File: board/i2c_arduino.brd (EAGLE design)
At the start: 36.5 x 55.9 mm, 20 parts, among them IC1 MEGA8-P

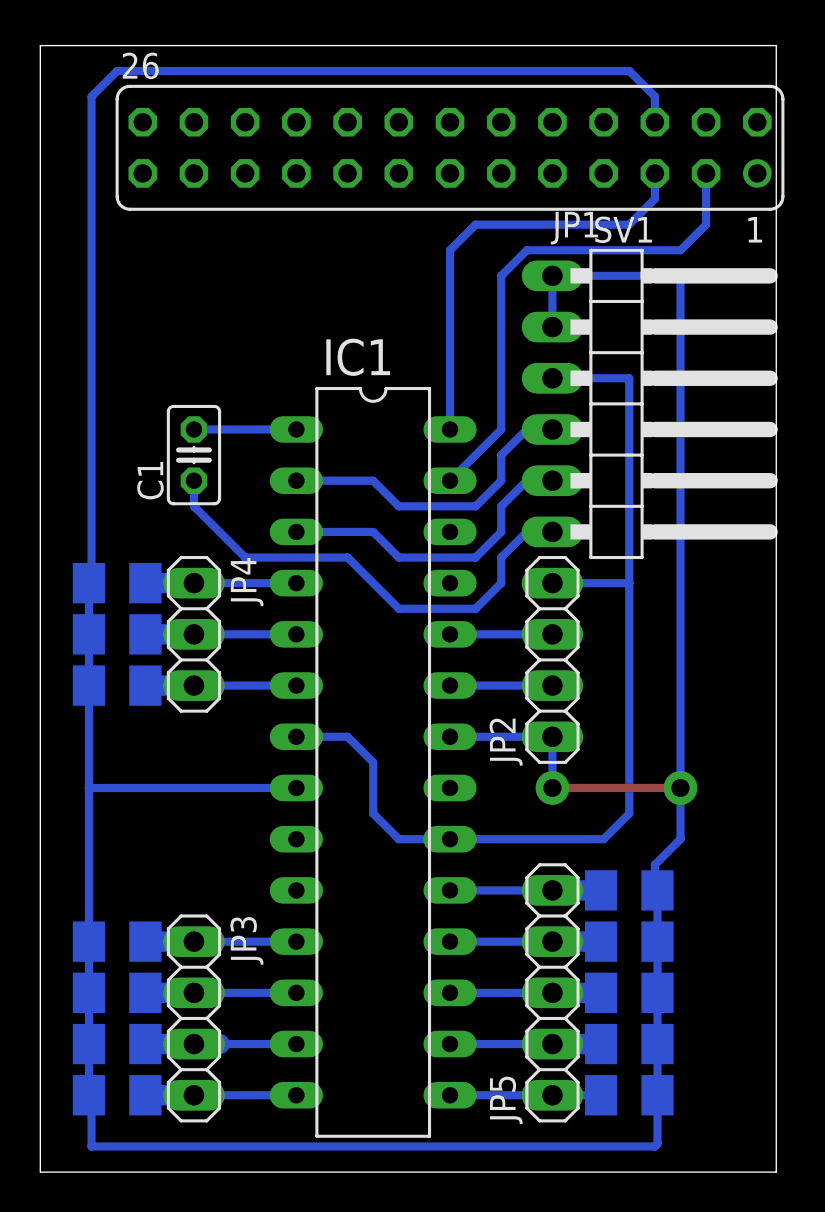
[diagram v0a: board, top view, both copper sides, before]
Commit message: Updated buttons handling
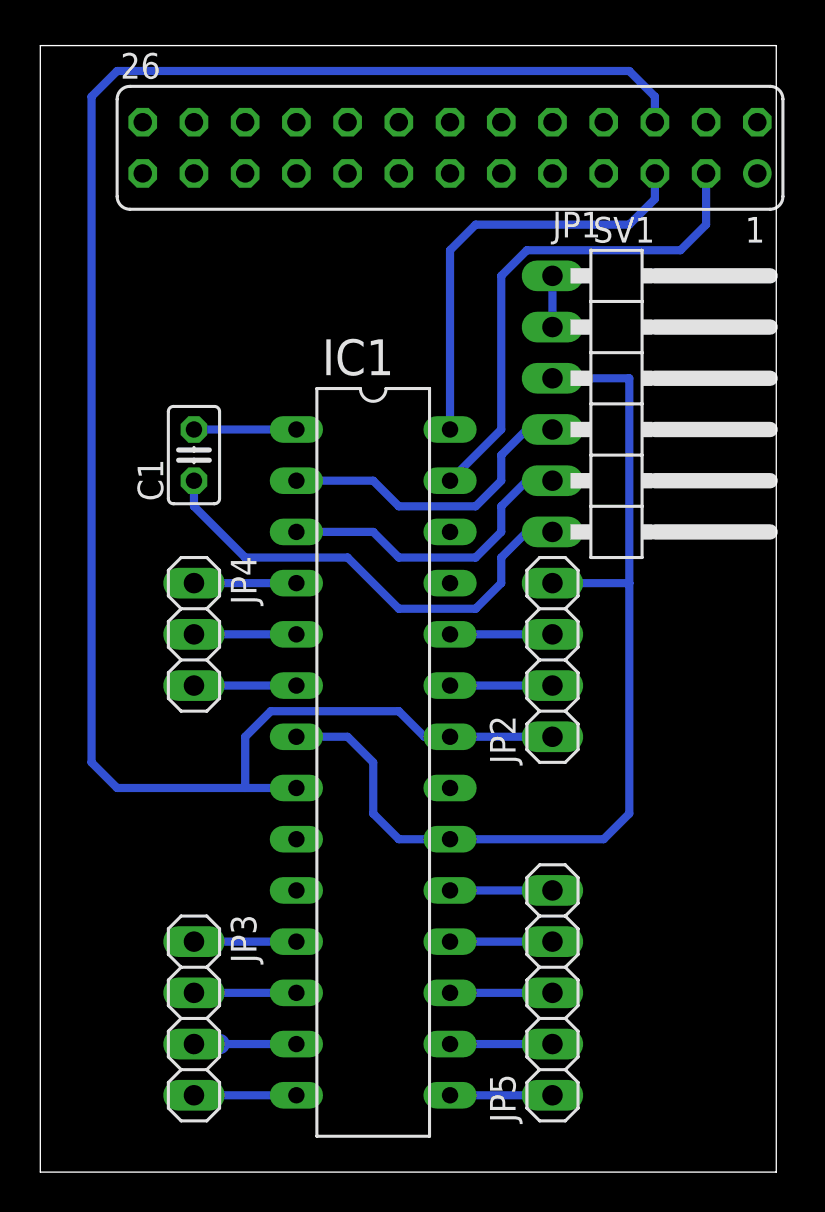
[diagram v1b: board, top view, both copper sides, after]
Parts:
- removed R1, R10, R11, R12, R2, R3, R4, R5, R6, R7, R8, R9: 10k, rcl:M1206
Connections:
- net GND: no longer R1.1, R10.1, R11.1, R12.1, R2.1, R3.1, R4.1, R5.1, R6.1, R7.1, R8.1, R9.1
- net IN10: no longer R9.2
- net IN11: no longer R10.2
- net IN12: no longer R11.2
- net IN13: no longer R12.2
- net IN2: no longer R1.2
- net IN3: no longer R3.2
- net IN4: no longer R2.2
- net IN5: no longer R4.2
- net IN6: no longer R5.2
- net IN7: no longer R6.2
- net IN8: no longer R7.2
- net IN9: no longer R8.2
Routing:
- net GND: track 187.3 -> 95.3 mm, vias 2 -> 0
- net IN9: track 7.49 -> 5.08 mm
- net IN8: track 7.49 -> 5.08 mm
- net IN7: track 8.76 -> 6.35 mm
- net IN6: track 7.49 -> 5.08 mm
- net IN5: track 7.49 -> 5.08 mm
- net IN4: track 7.49 -> 5.08 mm
- net IN3: track 7.49 -> 5.08 mm
- net IN2: track 7.49 -> 5.08 mm
- net IN13: track 7.49 -> 5.08 mm
- net IN12: track 7.49 -> 5.08 mm
- net IN11: track 7.49 -> 5.08 mm
- net IN10: track 7.49 -> 5.08 mm
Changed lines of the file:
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@@
 <attribute name="OC_FARNELL" value="unknown" x="20.32" y="50.8" size="1.778" layer="27" rot="R180" display="off"/>
 </element>
-<element name="R1" library="rcl" package="M1206" value="10k" x="3.81" y="29.21" rot="MR180"/>
-<element name="R2" library="rcl" package="M1206" value="10k" x="3.81" y="24.13" rot="MR180"/>
-<element name="R3" library="rcl" package="M1206" value="10k" x="3.81" y="26.67" rot="MR180"/>
-<element name="R4" library="rcl" package="M1206" value="10k" x="3.81" y="11.43" rot="MR180"/>
-<element name="R5" library="rcl" package="M1206" value="10k" x="3.81" y="8.89" rot="MR180"/>
-<element name="R6" library="rcl" package="M1206" value="10k" x="3.81" y="6.35" rot="MR180"/>
-<element name="R7" library="rcl" package="M1206" value="10k" x="3.81" y="3.81" rot="MR180"/>
-<element name="R8" library="rcl" package="M1206" value="10k" x="29.21" y="3.81" rot="MR0"/>
-<element name="R9" library="rcl" package="M1206" value="10k" x="29.21" y="6.35" rot="MR0"/>
-<element name="R10" library="rcl" package="M1206" value="10k" x="29.21" y="8.89" rot="MR0"/>
-<element name="R11" library="rcl" package="M1206" value="10k" x="29.21" y="11.43" rot="MR0"/>
-<element name="R12" library="rcl" package="M1206" value="10k" x="29.21" y="13.97" rot="MR0"/>
 <element name="JP2" library="pinhead" package="1X04" value="" x="25.4" y="25.4" rot="R90"/>
 <element name="JP3" library="pinhead" package="1X04" value="" x="7.62" y="7.62" rot="R270"/>
@@
 <contactref element="JP1" pad="1"/>
 <contactref element="IC1" pad="8"/>
-<contactref element="R1" pad="1"/>
-<contactref element="R12" pad="1"/>
-<contactref element="R11" pad="1"/>
-<contactref element="R10" pad="1"/>
-<contactref element="R3" pad="1"/>
-<contactref element="R2" pad="1"/>
-<contactref element="R4" pad="1"/>
-<contactref element="R5" pad="1"/>
-<contactref element="R6" pad="1"/>
-<contactref element="R7" pad="1"/>
-<contactref element="R8" pad="1"/>
-<contactref element="R9" pad="1"/>
-<wire x1="2.41" y1="3.81" x2="2.41" y2="6.35" width="0.4064" layer="16"/>
-<wire x1="2.41" y1="6.35" x2="2.41" y2="8.89" width="0.4064" layer="16"/>
-<wire x1="2.41" y1="8.89" x2="2.41" y2="11.43" width="0.4064" layer="16"/>
-<wire x1="2.41" y1="24.13" x2="2.41" y2="19.05" width="0.4064" layer="16"/>
-<wire x1="2.41" y1="19.05" x2="2.41" y2="11.43" width="0.4064" layer="16"/>
-<wire x1="2.41" y1="26.67" x2="2.41" y2="24.13" width="0.4064" layer="16"/>
-<wire x1="2.41" y1="29.21" x2="2.41" y2="26.67" width="0.4064" layer="16"/>
-<wire x1="30.61" y1="3.81" x2="30.61" y2="1.4" width="0.4064" layer="16"/>
-<wire x1="30.61" y1="1.4" x2="30.48" y2="1.27" width="0.4064" layer="16"/>
-<wire x1="30.48" y1="1.27" x2="2.54" y2="1.27" width="0.4064" layer="16"/>
-<wire x1="2.54" y1="1.27" x2="2.54" y2="3.68" width="0.4064" layer="16"/>
-<wire x1="2.54" y1="3.68" x2="2.41" y2="3.81" width="1.016" layer="16"/>
-<wire x1="12.7" y1="19.05" x2="2.41" y2="19.05" width="0.4064" layer="16"/>
 <contactref element="JP2" pad="1"/>
 <wire x1="25.4" y1="21.59" x2="20.32" y2="21.59" width="0.4064" layer="16"/>
 <contactref element="IC1" pad="22"/>
-<wire x1="2.54" y1="29.34" x2="2.41" y2="29.21" width="1.016" layer="16"/>
-<wire x1="30.61" y1="3.81" x2="30.61" y2="6.35" width="0.4064" layer="16"/>
-<wire x1="30.61" y1="6.35" x2="30.61" y2="8.89" width="0.4064" layer="16"/>
-<wire x1="30.61" y1="8.89" x2="30.61" y2="11.43" width="0.4064" layer="16"/>
-<wire x1="30.61" y1="11.43" x2="30.61" y2="13.97" width="0.4064" layer="16"/>
 <contactref element="SV1" pad="6"/>
 <wire x1="25.4" y1="44.45" x2="25.4" y2="41.91" width="0.4064" layer="16"/>
-<wire x1="31.75" y1="44.45" x2="25.4" y2="44.45" width="0.4064" layer="16"/>
-<wire x1="25.4" y1="21.59" x2="25.4" y2="19.05" width="0.4064" layer="16"/>
-<via x="25.4" y="19.05" extent="1-16" drill="0.9" diameter="1.6764" shape="octagon"/>
-<wire x1="25.4" y1="19.05" x2="31.75" y2="19.05" width="0.4064" layer="1"/>
-<via x="31.75" y="19.05" extent="1-16" drill="0.9" diameter="1.6764" shape="octagon"/>
-<wire x1="31.75" y1="19.05" x2="31.75" y2="44.45" width="0.4064" layer="16"/>
-<wire x1="31.75" y1="19.05" x2="31.75" y2="16.51" width="0.4064" layer="16"/>
-<wire x1="31.75" y1="16.51" x2="30.48" y2="15.24" width="0.4064" layer="16"/>
-<wire x1="30.48" y1="15.24" x2="30.48" y2="14.1" width="0.4064" layer="16"/>
-<wire x1="30.48" y1="14.1" x2="30.61" y2="13.97" width="0.4064" layer="16"/>
 <wire x1="30.48" y1="52.07" x2="30.48" y2="53.34" width="0.4064" layer="16"/>
 <wire x1="30.48" y1="53.34" x2="29.21" y2="54.61" width="0.4064" layer="16"/>
 <wire x1="29.21" y1="54.61" x2="3.81" y2="54.61" width="0.4064" layer="16"/>
 <wire x1="3.81" y1="54.61" x2="2.54" y2="53.34" width="0.4064" layer="16"/>
-<wire x1="2.54" y1="53.34" x2="2.54" y2="29.34" width="0.4064" layer="16"/>
+<wire x1="2.54" y1="53.34" x2="2.54" y2="20.32" width="0.4064" layer="16"/>
+<wire x1="12.7" y1="19.05" x2="10.16" y2="19.05" width="0.4064" layer="16"/>
+<wire x1="10.16" y1="19.05" x2="3.81" y2="19.05" width="0.4064" layer="16"/>
+<wire x1="3.81" y1="19.05" x2="2.54" y2="20.32" width="0.4064" layer="16"/>
+<wire x1="20.32" y1="21.59" x2="19.05" y2="21.59" width="0.4064" layer="16"/>
+<wire x1="19.05" y1="21.59" x2="17.78" y2="22.86" width="0.4064" layer="16"/>
+<wire x1="17.78" y1="22.86" x2="11.43" y2="22.86" width="0.4064" layer="16"/>
+<wire x1="11.43" y1="22.86" x2="10.16" y2="21.59" width="0.4064" layer="16"/>
+<wire x1="10.16" y1="21.59" x2="10.16" y2="19.05" width="0.4064" layer="16"/>
+<wire x1="30.48" y1="52.07" x2="25.4" y2="44.45" width="0" layer="19" extent="1-1"/>
 </signal>
 <signal name="VCC">
@@
 <signal name="IN6">
 <contactref element="IC1" pad="12"/>
-<contactref element="R5" pad="2"/>
 <contactref element="JP3" pad="2"/>
-<wire x1="5.21" y1="8.89" x2="7.62" y2="8.89" width="1.016" layer="16"/>
 <wire x1="7.62" y1="8.89" x2="12.7" y2="8.89" width="0.4064" layer="16"/>
 </signal>
 <signal name="IN7">
 <contactref element="IC1" pad="13"/>
-<contactref element="R6" pad="2"/>
 <contactref element="JP3" pad="3"/>
-<wire x1="5.21" y1="6.35" x2="7.62" y2="6.35" width="1.016" layer="16"/>
 <wire x1="8.89" y1="6.35" x2="7.62" y2="6.35" width="1.016" layer="16"/>
 <wire x1="7.62" y1="6.35" x2="12.7" y2="6.35" width="0.4064" layer="16"/>
@@
 <signal name="IN8">
 <contactref element="IC1" pad="14"/>
-<contactref element="R7" pad="2"/>
 <contactref element="JP3" pad="4"/>
-<wire x1="5.21" y1="3.81" x2="7.62" y2="3.81" width="1.016" layer="16"/>
 <wire x1="7.62" y1="3.81" x2="12.7" y2="3.81" width="0.4064" layer="16"/>
 </signal>
 <signal name="IN9">
 <contactref element="IC1" pad="15"/>
-<contactref element="R8" pad="2"/>
 <contactref element="JP5" pad="1"/>
 <wire x1="20.32" y1="3.81" x2="25.4" y2="3.81" width="0.4064" layer="16"/>
-<wire x1="25.4" y1="3.81" x2="27.81" y2="3.81" width="0.4064" layer="16"/>
 </signal>
 <signal name="IN10">
 <contactref element="IC1" pad="16"/>
-<contactref element="R9" pad="2"/>
 <contactref element="JP5" pad="2"/>
-<wire x1="27.81" y1="6.35" x2="25.4" y2="6.35" width="1.016" layer="16"/>
 <wire x1="25.4" y1="6.35" x2="20.32" y2="6.35" width="0.4064" layer="16"/>
 </signal>
 <signal name="IN11">
 <contactref element="IC1" pad="17"/>
-<contactref element="R10" pad="2"/>
 <contactref element="JP5" pad="3"/>
 <wire x1="25.4" y1="8.89" x2="20.32" y2="8.89" width="0.4064" layer="16"/>
-<wire x1="25.4" y1="8.89" x2="27.81" y2="8.89" width="1.016" layer="16"/>
 </signal>
 <signal name="IN12">
 <contactref element="IC1" pad="18"/>
-<contactref element="R11" pad="2"/>
 <contactref element="JP5" pad="4"/>
-<wire x1="27.81" y1="11.43" x2="25.4" y2="11.43" width="1.016" layer="16"/>
 <wire x1="25.4" y1="11.43" x2="20.32" y2="11.43" width="0.4064" layer="16"/>
 </signal>
 <signal name="IN13">
 <contactref element="IC1" pad="19"/>
-<contactref element="R12" pad="2"/>
 <contactref element="JP5" pad="5"/>
 <wire x1="20.32" y1="13.97" x2="25.4" y2="13.97" width="0.4064" layer="16"/>
-<wire x1="25.4" y1="13.97" x2="27.81" y2="13.97" width="1.016" layer="16"/>
 </signal>
 <signal name="N$15">
@@
 </signal>
 <signal name="IN5">
-<contactref element="R4" pad="2"/>
 <contactref element="IC1" pad="11"/>
 <contactref element="JP3" pad="1"/>
-<wire x1="5.21" y1="11.43" x2="7.62" y2="11.43" width="1.016" layer="16"/>
 <wire x1="7.62" y1="11.43" x2="12.7" y2="11.43" width="0.4064" layer="16"/>
 </signal>
@@
 <contactref element="JP4" pad="1"/>
 <contactref element="IC1" pad="4"/>
-<contactref element="R1" pad="2"/>
 <wire x1="12.7" y1="29.21" x2="7.62" y2="29.21" width="0.4064" layer="16"/>
-<wire x1="7.62" y1="29.21" x2="5.21" y2="29.21" width="1.016" layer="16"/>
 </signal>
 <signal name="IN3">
 <contactref element="JP4" pad="2"/>
 <contactref element="IC1" pad="5"/>
-<contactref element="R3" pad="2"/>
 <wire x1="7.62" y1="26.67" x2="12.7" y2="26.67" width="0.4064" layer="16"/>
-<wire x1="7.62" y1="26.67" x2="5.21" y2="26.67" width="1.016" layer="16"/>
 </signal>
 <signal name="IN4">
 <contactref element="JP4" pad="3"/>
 <contactref element="IC1" pad="6"/>
-<contactref element="R2" pad="2"/>
-<wire x1="5.21" y1="24.13" x2="7.62" y2="24.13" width="1.016" layer="16"/>
 <wire x1="7.62" y1="24.13" x2="12.7" y2="24.13" width="0.4064" layer="16"/>
 </signal>
